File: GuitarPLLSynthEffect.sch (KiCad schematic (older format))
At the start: 14 parts

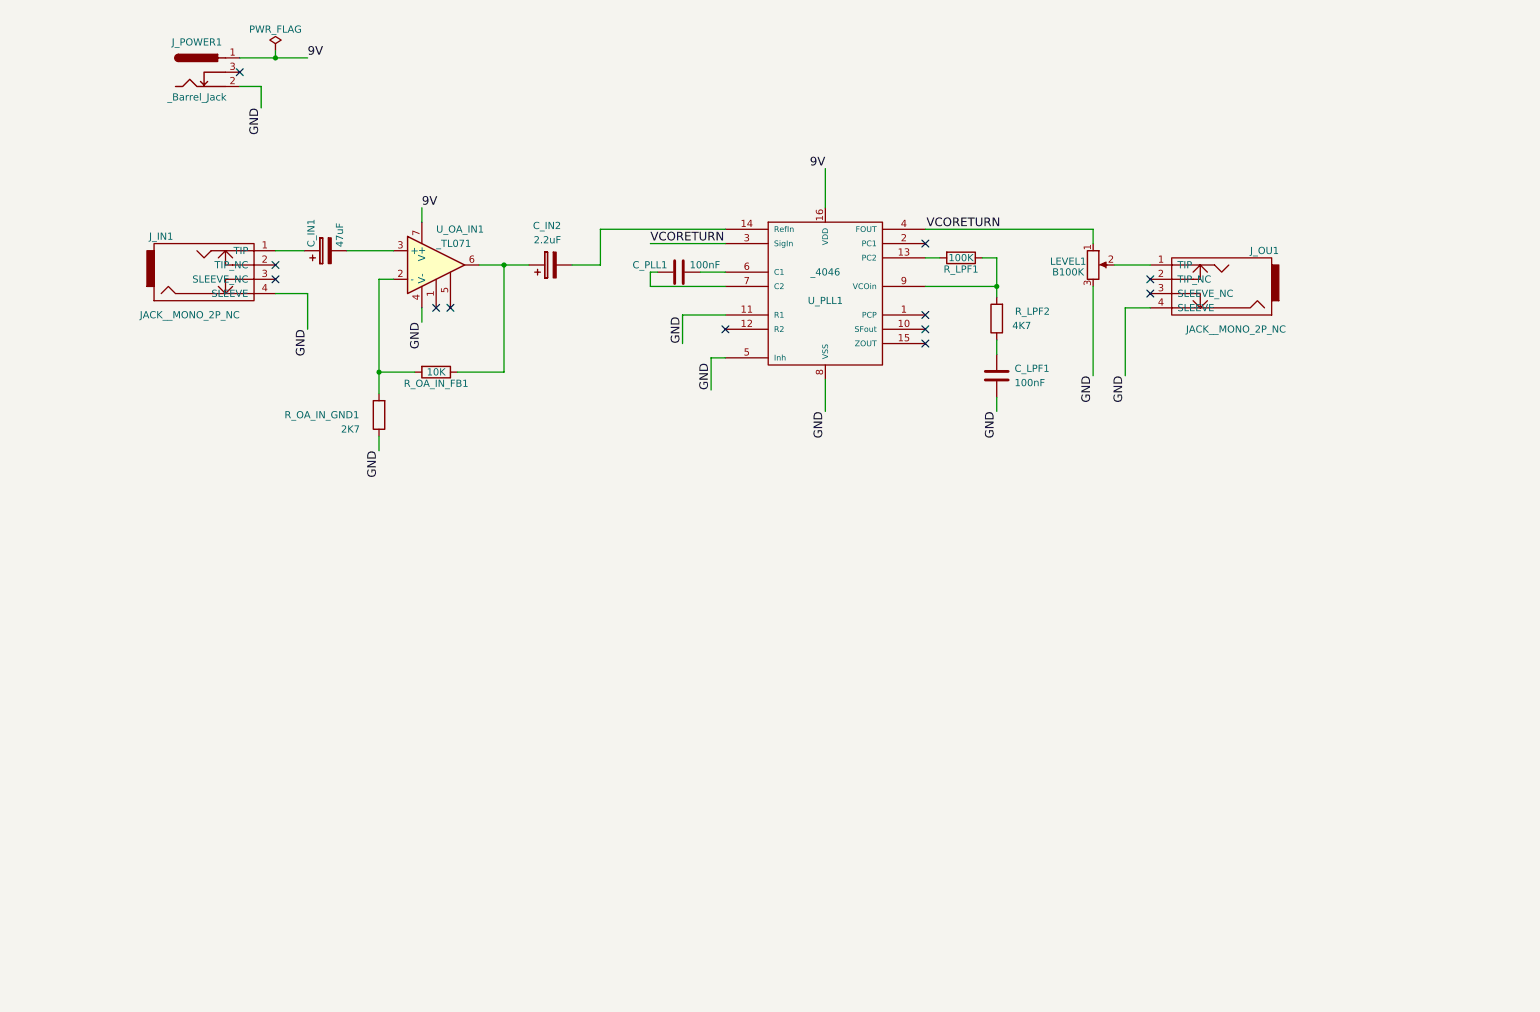
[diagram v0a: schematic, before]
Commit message: Schematic design update
- Added PLL controls
- Added dual power supply (TC7662B)
- Added Output buffer OpAmp
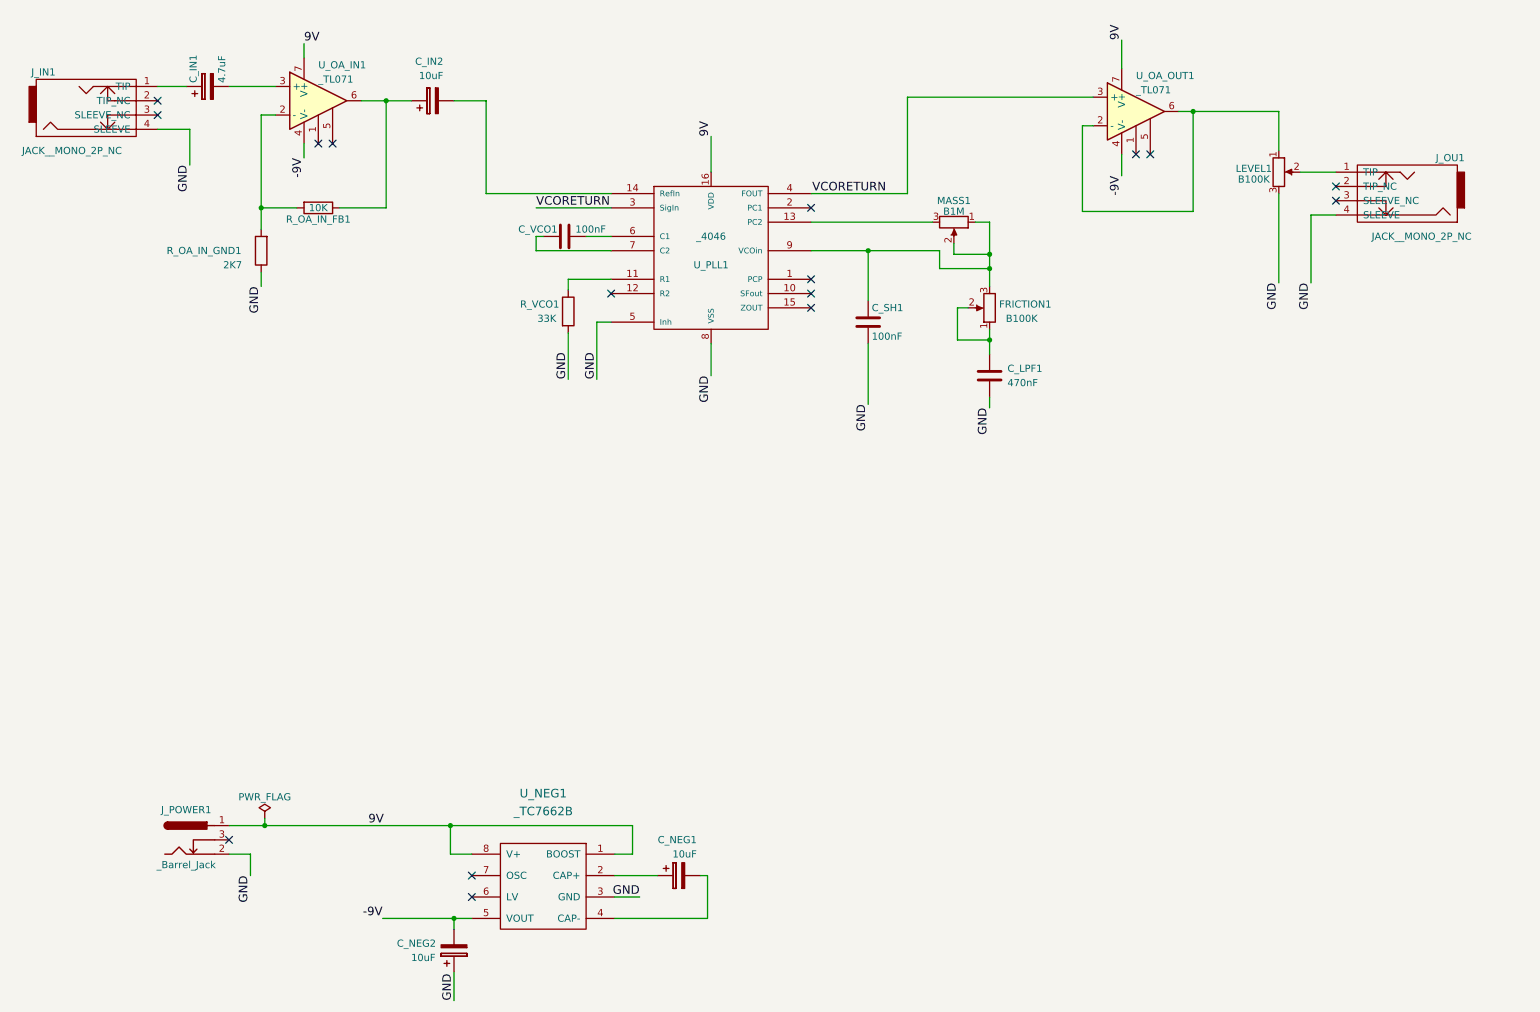
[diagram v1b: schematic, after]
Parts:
- removed R_LPF1: 100K, symbol R
- removed R_LPF2: 4K7, symbol R
- added C_NEG1, C_NEG2: 10uF, symbol CP
- added C_SH1: 100nF, symbol C
- added FRICTION1: B100K, symbol NPOT
- added MASS1: B1M, symbol NPOT
- added R_VCO1: 33K, symbol R
- added U_NEG1: _TC7662B, symbol _TC7662B
- added U_OA_OUT1: _TL071, symbol _TL071
- C_IN1: value 47uF -> 4.7uF
- C_IN2: value 2.2uF -> 10uF
- C_LPF1: value 100nF -> 470nF
- renumbered C_PLL1 to C_VCO1
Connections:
- net 9V: now also U_NEG1.1 (BOOST), U_NEG1.8 (V+), U_OA_OUT1.7 (V+)
- net GND: now also C_NEG2.1, C_SH1.2, R_VCO1.2, U_NEG1.3 (GND); no longer U_OA_IN1.4 (V-), U_PLL1.11 (R1)
- net VCORETURN: now also U_OA_OUT1.3 (+); no longer LEVEL1.1
- net at U_PLL1.13 (PC2): now also MASS1.3
- net at U_PLL1.9 (VCOin): now also C_SH1.1, FRICTION1.3, MASS1.1, MASS1.2
- net at C_LPF1.1: now also FRICTION1.1, FRICTION1.2
- new net: R_VCO1.1, U_PLL1.11 (R1)
- new net: LEVEL1.1, U_OA_OUT1.2 (-), U_OA_OUT1.6
- new net: C_NEG1.1, U_NEG1.2 (CAP+)
- new net: C_NEG1.2, U_NEG1.4 (CAP-)
- new net -9V: C_NEG2.2, U_NEG1.5 (VOUT), U_OA_IN1.4 (V-), U_OA_OUT1.4 (V-)
- no-connect marks 12 -> 16
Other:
- moved on the sheet: C_IN1, C_IN2, C_LPF1, C_VCO1, J_IN1, J_OU1, J_POWER1, LEVEL1, R_OA_IN_FB1, R_OA_IN_GND1, U_OA_IN1, U_PLL1

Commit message: Schematic design update
- Added fx trigger/gain control to OAFX_IN opamp
- Added FM control to PLL
- Added clean/fx summing opamp
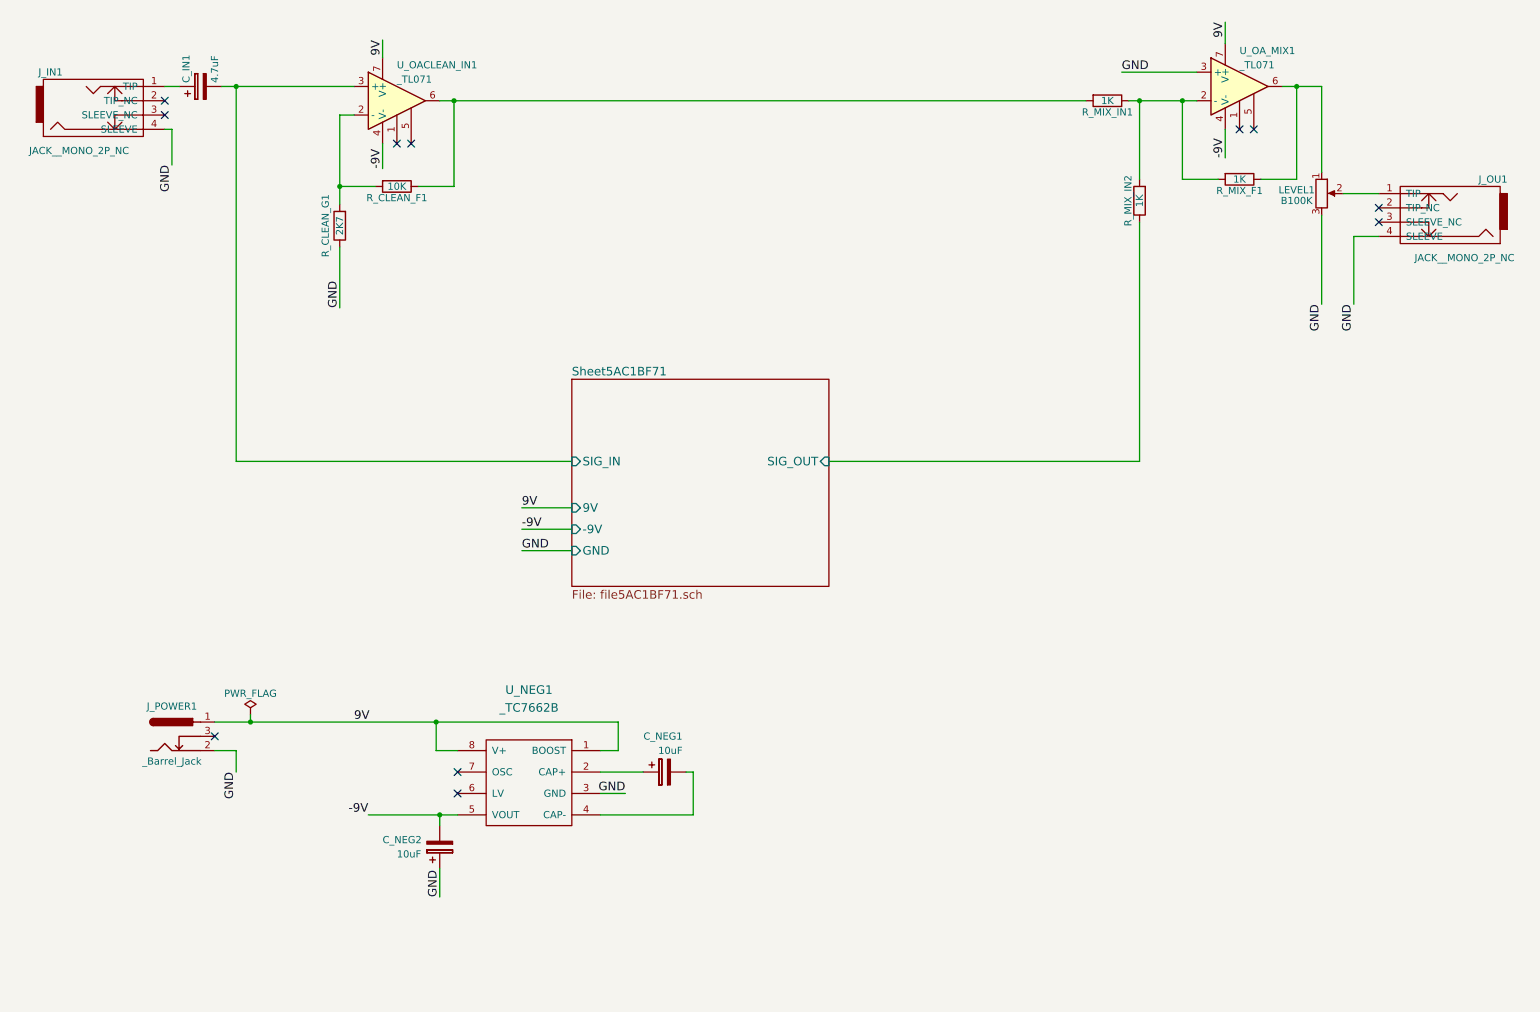
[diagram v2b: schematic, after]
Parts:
- removed C_IN2: 10uF, symbol CP
- removed C_LPF1: 470nF, symbol C
- removed C_SH1, C_VCO1: 100nF, symbol C
- removed FRICTION1: B100K, symbol NPOT
- removed MASS1: B1M, symbol NPOT
- removed R_OA_IN_FB1: 10K, symbol R
- removed R_OA_IN_GND1: 2K7, symbol R
- removed R_VCO1: 33K, symbol R
- removed U_OA_IN1, U_OA_OUT1: _TL071, symbol _TL071
- removed U_PLL1: _4046, symbol _4046
- added R_CLEAN_F1: 10K, symbol R
- added R_CLEAN_G1: 2K7, symbol R
- added R_MIX_F1, R_MIX_IN1, R_MIX_IN2: 1K, symbol R
- added U_OACLEAN_IN1, U_OA_MIX1: _TL071, symbol _TL071
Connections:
- net -9V: now also U_OACLEAN_IN1.4 (V-), U_OA_MIX1.4 (V-)
- net 9V: now also U_OACLEAN_IN1.7 (V+), U_OA_MIX1.7 (V+)
- net GND: now also R_CLEAN_G1.1, U_OA_MIX1.3 (+)
- net Sheet5AC1BF71/SIG_IN: now reaches C_IN1.2
- net Sheet5AC1BF71/SIG_IN: now also U_OACLEAN_IN1.3 (+)
- net at LEVEL1.1: now also R_MIX_F1.1, U_OA_MIX1.6
- new net: R_MIX_F1.2, R_MIX_IN1.1, R_MIX_IN2.2, U_OA_MIX1.2 (-)
- new net: R_CLEAN_F1.2, R_CLEAN_G1.2, U_OACLEAN_IN1.2 (-)
- new net: R_CLEAN_F1.1, R_MIX_IN1.2, U_OACLEAN_IN1.6
- new net Sheet5AC1BF71/SIG_OUT: R_MIX_IN2.1
- no-connect marks 16 -> 11
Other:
- moved on the sheet: C_IN1, C_NEG1, C_NEG2, J_IN1, J_OU1, J_POWER1, LEVEL1, U_NEG1

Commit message: UPDATE
ADDED FX OUPUT GAIN STAGE
ADDED FX/CLEAN MIXER OPAMP (WITH SINGLE BLEND POT CONTROL)
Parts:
- removed LEVEL1: B100K, symbol NPOT
- removed R_CLEAN_F1: 10K, symbol R
- removed R_CLEAN_G1: 2K7, symbol R
- removed R_MIX_IN1, R_MIX_IN2: 1K, symbol R
- added MIX1: B100K, symbol NPOT
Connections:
- net Sheet5AC1BF71/SIG_OUT: now also MIX1.3
- net at J_OU1.1 (TIP): now also R_MIX_F1.1, U_OA_MIX1.6
- net at R_MIX_F1.2, U_OA_MIX1.2 (-): now also MIX1.2
- net at U_OACLEAN_IN1.2 (-): now also U_OACLEAN_IN1.6, MIX1.1
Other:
- moved on the sheet: J_OU1, R_MIX_F1, U_OA_MIX1
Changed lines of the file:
@@
 L JACK__MONO_2P_NC J_OU1
 U 1 1 5ABD53E5
-P 10550 2075
-F 0 "J_OU1" H 10200 1875 50  0000 C CNN
-F 1 "JACK__MONO_2P_NC" H 10400 2425 50  0000 C CNN
-F 2 "" H 10550 2075 50  0001 C CNN
-F 3 "" H 10550 2075 50  0001 C CNN
-	1    10550 2075
+P 10475 2625
+F 0 "J_OU1" H 10125 2425 50  0000 C CNN
+F 1 "JACK__MONO_2P_NC" H 10325 2975 50  0000 C CNN
+F 2 "" H 10475 2625 50  0001 C CNN
+F 3 "" H 10475 2625 50  0001 C CNN
+	1    10475 2625
 	-1   0    0    1
 $EndComp
@@
 NoConn ~ 1600 1425
 NoConn ~ 1950 5775
-NoConn ~ 10100 2075
-NoConn ~ 10100 2175
+NoConn ~ 10025 2625
+NoConn ~ 10025 2725
 $Comp
 L CP C_IN1
@@
 Wire Wire Line
 	1600 1225 1700 1225
-$Comp
-L NPOT LEVEL1
-U 1 1 5ABD68E0
-P 9700 1975
-F 0 "LEVEL1" H 9525 2000 50  0000 C CNN
-F 1 "B100K" H 9525 1925 50  0000 C CNN
-F 2 "" H 9700 1975 50  0001 C CNN
-F 3 "" H 9700 1975 50  0001 C CNN
-	1    9700 1975
-	1    0    0    -1
-$EndComp
-Wire Wire Line
-	9700 2125 9700 2750
-Text Label 9700 2750 3    60   ~ 0
-GND
-Wire Wire Line
-	9850 1975 10100 1975
-Wire Wire Line
-	10100 2275 9925 2275
-Wire Wire Line
-	9925 2275 9925 2750
-Text Label 9925 2750 3    60   ~ 0
+Wire Wire Line
+	9625 2525 10025 2525
+Wire Wire Line
+	10025 2825 9850 2825
+Wire Wire Line
+	9850 2825 9850 3300
+Text Label 9850 3300 3    60   ~ 0
 GND
 $Comp
@@
 L _TL071 U_OA_MIX1
 U 1 1 5AC053DF
-P 9125 1225
-F 0 "U_OA_MIX1" H 9125 1475 50  0000 L CNN
-F 1 "_TL071" H 9125 1375 50  0000 L CNN
-F 2 "" H 9175 1275 50  0001 C CNN
-F 3 "" H 9275 1375 50  0001 C CNN
-	1    9125 1225
+P 9050 1775
+F 0 "U_OA_MIX1" H 9050 2025 50  0000 L CNN
+F 1 "_TL071" H 9050 1925 50  0000 L CNN
+F 2 "" H 9100 1825 50  0001 C CNN
+F 3 "" H 9200 1925 50  0001 C CNN
+	1    9050 1775
 	1    0    0    -1
 $EndComp
@@
 	2925 1425 2825 1425
 Wire Wire Line
-	2825 1425 2825 2050
-Wire Wire Line
-	2825 1925 3075 1925
-$Comp
-L R R_CLEAN_F1
-U 1 1 5AC0A252
-P 3225 1925
-F 0 "R_CLEAN_F1" V 3305 1925 50  0000 C CNN
-F 1 "10K" V 3225 1925 50  0000 C CNN
-F 2 "" V 3155 1925 50  0001 C CNN
-F 3 "" H 3225 1925 50  0001 C CNN
-	1    3225 1925
-	0    1    1    0
-$EndComp
-Wire Wire Line
-	3375 1925 3625 1925
-Wire Wire Line
 	3625 1925 3625 1325
 Wire Wire Line
-	3525 1325 8050 1325
-$Comp
-L R R_CLEAN_G1
-U 1 1 5AC0AA0C
-P 2825 2200
-F 0 "R_CLEAN_G1" V 2925 2200 50  0000 C CNN
-F 1 "2K7" V 2825 2200 50  0000 C CNN
-F 2 "" V 2755 2200 50  0001 C CNN
-F 3 "" H 2825 2200 50  0001 C CNN
-	1    2825 2200
-	-1   0    0    1
-$EndComp
-Connection ~ 2825 1925
-Wire Wire Line
-	2825 2350 2825 2775
-Text Label 2825 2775 1    60   ~ 0
-GND
-Wire Wire Line
-	8300 1125 8825 1125
-Wire Wire Line
-	9025 1525 9025 1725
-Wire Wire Line
-	9025 925  9025 775
-Wire Wire Line
-	8425 1875 8425 1325
-Wire Wire Line
-	8350 1325 8825 1325
-Wire Wire Line
-	8725 1325 8725 1875
-Wire Wire Line
-	8725 1875 8975 1875
-Connection ~ 8725 1325
+	3525 1325 7950 1325
+Wire Wire Line
+	8225 1675 8750 1675
+Wire Wire Line
+	8950 2075 8950 2275
+Wire Wire Line
+	8950 1475 8950 1325
+Wire Wire Line
+	8100 1875 8750 1875
+Wire Wire Line
+	8650 1875 8650 2425
+Wire Wire Line
+	8650 2425 8900 2425
+Connection ~ 8650 1875
 $Comp
 L R R_MIX_F1
 U 1 1 5AC0CCCD
-P 9125 1875
-F 0 "R_MIX_F1" V 9205 1875 50  0000 C CNN
-F 1 "1K" V 9125 1875 50  0000 C CNN
-F 2 "" V 9055 1875 50  0001 C CNN
-F 3 "" H 9125 1875 50  0001 C CNN
-	1    9125 1875
+P 9050 2425
+F 0 "R_MIX_F1" V 9130 2425 50  0000 C CNN
+F 1 "1K" V 9050 2425 50  0000 C CNN
+F 2 "" V 8980 2425 50  0001 C CNN
+F 3 "" H 9050 2425 50  0001 C CNN
+	1    9050 2425
 	0    1    1    0
 $EndComp
 Wire Wire Line
-	9275 1875 9525 1875
-Wire Wire Line
-	9525 1875 9525 1225
-Wire Wire Line
-	9425 1225 9700 1225
-Text Label 8300 1125 0    60   ~ 0
-GND
-Text Label 9025 1725 1    60   ~ 0
--9V
-Text Label 9025 775  3    60   ~ 0
-9V
-Connection ~ 8425 1325
-$Comp
-L R R_MIX_IN1
-U 1 1 5AC0D344
-P 8200 1325
-F 0 "R_MIX_IN1" V 8280 1325 50  0000 C CNN
-F 1 "1K" V 8200 1325 50  0000 C CNN
-F 2 "" V 8130 1325 50  0001 C CNN
-F 3 "" H 8200 1325 50  0001 C CNN
-	1    8200 1325
-	0    1    1    0
-$EndComp
-$Comp
-L R R_MIX_IN2
-U 1 1 5AC0D3F4
-P 8425 2025
-F 0 "R_MIX_IN2" V 8505 2025 50  0000 C CNN
-F 1 "1K" V 8425 2025 50  0000 C CNN
-F 2 "" V 8355 2025 50  0001 C CNN
-F 3 "" H 8425 2025 50  0001 C CNN
-	1    8425 2025
-	-1   0    0    1
-$EndComp
-Wire Wire Line
-	9700 1225 9700 1825
-Connection ~ 9525 1225
+	9200 2425 9450 2425
+Wire Wire Line
+	9450 2425 9450 1775
+Wire Wire Line
+	9350 1775 9625 1775
+Text Label 8225 1675 0    60   ~ 0
+GND
+Text Label 8950 2275 1    60   ~ 0
+-9V
+Text Label 8950 1325 3    60   ~ 0
+9V
+Wire Wire Line
+	9625 1775 9625 2525
+Connection ~ 9450 1775
 Connection ~ 3625 1325
 $Sheet
@@
 	2100 3850 2100 1225
 Wire Wire Line
-	6250 3850 8425 3850
-Wire Wire Line
-	8425 3850 8425 2175
+	6250 3850 7950 3850
+Wire Wire Line
+	7950 3850 7950 2025
 Wire Wire Line
 	4450 4175 4100 4175
@@
 Text Label 4100 4475 0    60   ~ 0
 GND
-NoConn ~ 9125 1525
-NoConn ~ 9225 1525
+NoConn ~ 9050 2075
+NoConn ~ 9150 2075
+Wire Wire Line
+	3625 1925 2825 1925
+Wire Wire Line
+	2825 1925 2825 1425
+$Comp
+L NPOT MIX1
+U 1 1 5AC12327
+P 7950 1875
+F 0 "MIX1" V 7775 1875 50  0000 C CNN
+F 1 "B100K" V 7850 1875 50  0000 C CNN
+F 2 "" H 7950 1875 50  0001 C CNN
+F 3 "" H 7950 1875 50  0001 C CNN
+	1    7950 1875
+	1    0    0    -1
+$EndComp
+Wire Wire Line
+	7950 1325 7950 1725
 $EndSCHEMATC

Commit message: UPDATE
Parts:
- added FXVOL1: B1K, symbol NPOT
- added R_FXVOL1: 560R, symbol R
- added R_MIX_G1: 10K, symbol R
- added U_OA_FXVOL1: _TL071, symbol _TL071
- R_MIX_F1: value 1K -> 10K
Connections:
- net -9V: now also U_OA_FXVOL1.4 (V-)
- net 9V: now also U_OA_FXVOL1.7 (V+)
- net GND: now also R_FXVOL1.2, R_MIX_G1.1; no longer U_OA_MIX1.3 (+)
- net Sheet5AC1BF71/SIG_OUT: now also U_OA_FXVOL1.3 (+); no longer MIX1.3
- net at R_MIX_F1.2, U_OA_MIX1.2 (-): now also R_MIX_G1.2; no longer MIX1.2
- net at U_OACLEAN_IN1.2 (-), U_OACLEAN_IN1.6: now also MIX1.3; no longer MIX1.1
- new net: MIX1.2, U_OA_MIX1.3 (+)
- new net: FXVOL1.3, MIX1.1, U_OA_FXVOL1.6
- new net: FXVOL1.1, FXVOL1.2, R_FXVOL1.1, U_OA_FXVOL1.2 (-)
- no-connect marks 11 -> 13
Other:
- note added: "GAIN = 1.0-2.79"
- moved on the sheet: MIX1
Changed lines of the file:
@@
 	3525 1325 7950 1325
-Wire Wire Line
-	8225 1675 8750 1675
 Wire Wire Line
 	8950 2075 8950 2275
@@
 	8950 1475 8950 1325
 Wire Wire Line
-	8100 1875 8750 1875
+	8650 1875 8750 1875
 Wire Wire Line
-	8650 1875 8650 2425
+	8650 1875 8650 2550
 Wire Wire Line
 	8650 2425 8900 2425
-Connection ~ 8650 1875
 $Comp
 L R R_MIX_F1
@@
 P 9050 2425
 F 0 "R_MIX_F1" V 9130 2425 50  0000 C CNN
-F 1 "1K" V 9050 2425 50  0000 C CNN
+F 1 "10K" V 9050 2425 50  0000 C CNN
 F 2 "" V 8980 2425 50  0001 C CNN
 F 3 "" H 9050 2425 50  0001 C CNN
@@
 Wire Wire Line
 	9350 1775 9625 1775
-Text Label 8225 1675 0    60   ~ 0
-GND
 Text Label 8950 2275 1    60   ~ 0
 -9V
@@
 	2100 3850 2100 1225
 Wire Wire Line
-	6250 3850 7950 3850
-Wire Wire Line
-	7950 3850 7950 2025
+	7950 3950 7950 1825
 Wire Wire Line
 	4450 4175 4100 4175
@@
 L NPOT MIX1
 U 1 1 5AC12327
-P 7950 1875
-F 0 "MIX1" V 7775 1875 50  0000 C CNN
-F 1 "B100K" V 7850 1875 50  0000 C CNN
-F 2 "" H 7950 1875 50  0001 C CNN
-F 3 "" H 7950 1875 50  0001 C CNN
-	1    7950 1875
+P 7950 1675
+F 0 "MIX1" V 7775 1675 50  0000 C CNN
+F 1 "B100K" V 7850 1675 50  0000 C CNN
+F 2 "" H 7950 1675 50  0001 C CNN
+F 3 "" H 7950 1675 50  0001 C CNN
+	1    7950 1675
+	1    0    0    1
+$EndComp
+Wire Wire Line
+	7950 1325 7950 1525
+Wire Wire Line
+	8100 1675 8750 1675
+$Comp
+L R R_MIX_G1
+U 1 1 5AC11ECA
+P 8650 2700
+F 0 "R_MIX_G1" V 8730 2700 50  0000 C CNN
+F 1 "10K" V 8650 2700 50  0000 C CNN
+F 2 "" V 8580 2700 50  0001 C CNN
+F 3 "" H 8650 2700 50  0001 C CNN
+	1    8650 2700
+	-1   0    0    1
+$EndComp
+Connection ~ 8650 2425
+Wire Wire Line
+	8650 2850 8650 3100
+Text Label 8650 3100 1    60   ~ 0
+GND
+$Comp
+L _TL071 U_OA_FXVOL1
+U 1 1 5AC1482A
+P 7025 3950
+F 0 "U_OA_FXVOL1" H 7025 4200 50  0000 L CNN
+F 1 "_TL071" H 7025 4100 50  0000 L CNN
+F 2 "" H 7075 4000 50  0001 C CNN
+F 3 "" H 7175 4100 50  0001 C CNN
+	1    7025 3950
 	1    0    0    -1
 $EndComp
 Wire Wire Line
-	7950 1325 7950 1725
+	6250 3850 6725 3850
+$Comp
+L NPOT FXVOL1
+U 1 1 5AC14DA8
+P 7250 4650
+F 0 "FXVOL1" V 7075 4650 50  0000 C CNN
+F 1 "B1K" V 7150 4650 50  0000 C CNN
+F 2 "" H 7250 4650 50  0001 C CNN
+F 3 "" H 7250 4650 50  0001 C CNN
+	1    7250 4650
+	0    -1   1    0
+$EndComp
+Wire Wire Line
+	6725 4050 6600 4050
+Wire Wire Line
+	6600 4050 6600 4750
+Wire Wire Line
+	6600 4650 7100 4650
+Wire Wire Line
+	7400 4650 7500 4650
+Wire Wire Line
+	7500 4650 7500 3950
+Wire Wire Line
+	7325 3950 7950 3950
+Connection ~ 7500 3950
+Wire Wire Line
+	7000 4650 7000 4900
+Wire Wire Line
+	7000 4900 7250 4900
+Wire Wire Line
+	7250 4900 7250 4800
+Connection ~ 7000 4650
+Wire Wire Line
+	6925 3650 6925 3500
+Wire Wire Line
+	6925 4250 6925 4475
+Connection ~ 6600 4650
+$Comp
+L R R_FXVOL1
+U 1 1 5AC151DA
+P 6600 4900
+F 0 "R_FXVOL1" V 6680 4900 50  0000 C CNN
+F 1 "560R" V 6600 4900 50  0000 C CNN
+F 2 "" V 6530 4900 50  0001 C CNN
+F 3 "" H 6600 4900 50  0001 C CNN
+	1    6600 4900
+	1    0    0    -1
+$EndComp
+Wire Wire Line
+	6600 5050 6600 5250
+Text Label 6600 5250 1    60   ~ 0
+GND
+Text Label 6925 4475 1    60   ~ 0
+-9V
+Text Label 6925 3500 3    60   ~ 0
+9V
+NoConn ~ 7025 4250
+NoConn ~ 7125 4250
+Text Notes 6875 5125 0    60   ~ 0
+GAIN = 1.0-2.79
 $EndSCHEMATC
